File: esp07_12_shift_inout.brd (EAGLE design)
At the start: 100 x 45 mm, 47 parts, among them IC1 74HCT595D, IC2 74HCT595D, IC3 74HC165D, IC4 74HC165D

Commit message: First version vhich will go to production
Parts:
- moved JP11 10.2 mm to (3.17, 6.35)
- moved JP12 10.2 mm to (3.17, 8.89)
- moved JP7 10.2 mm to (3.17, 2.54)
- moved JP10 8.25 mm to (3.17, 12.7)
- moved JP8 8.25 mm to (3.17, 33.0)
- moved JP9 8.25 mm to (3.17, 43.2)
- moved R3 1.91 mm to (62.2, 42.5)
- moved C1 1.91 mm to (29.8, 7.62)
- moved C3 1.91 mm to (32.4, 7.62)
- moved C4 1.91 mm to (21.0, 5.08)
- moved C5 1.91 mm to (26.0, 5.08)
- moved D1 1.91 mm to (17.1, 5.08)
- moved IC1 1.91 mm to (58.4, 12.1)
- moved IC2 1.91 mm to (81.3, 12.1)
- moved IC3 1.91 mm to (58.4, 26.0)
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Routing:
- net VCC: track 318.1 -> 330.8 mm
- net GPIO16: track 31.6 -> 41.9 mm
- net VCC-5V: track 9.36 -> 18.5 mm
- net CH_PD: track 26.8 -> 34.6 mm
- net GPIO0: track 30.9 -> 38.6 mm
- net GPIO2: track 30.5 -> 37.5 mm
- net RXD: track 21.3 -> 27.6 mm
- net TXD: track 17.2 -> 23.1 mm
- net GPIO15: track 51.0 -> 55.9 mm
- net GND: track 328.2 -> 332.7 mm
- net SCK: track 122.5 -> 124.3 mm
- net IN_LATCH: track 91.6 -> 92.8 mm
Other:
- board size 100 x 45 mm -> 97 x 45 mm

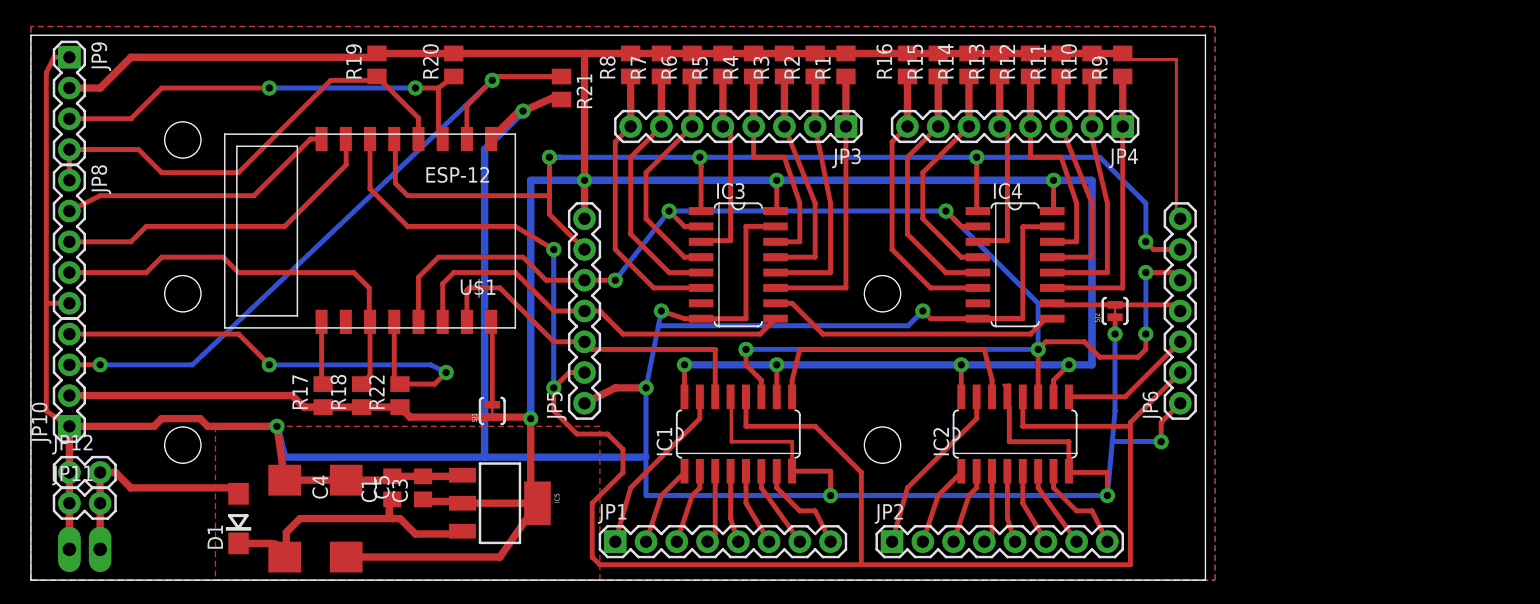
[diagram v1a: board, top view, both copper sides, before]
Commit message: * Change ESP module to ESP-12E footprint. Change ESP resistors to 0603. Change *_LATCH pins to 15,16
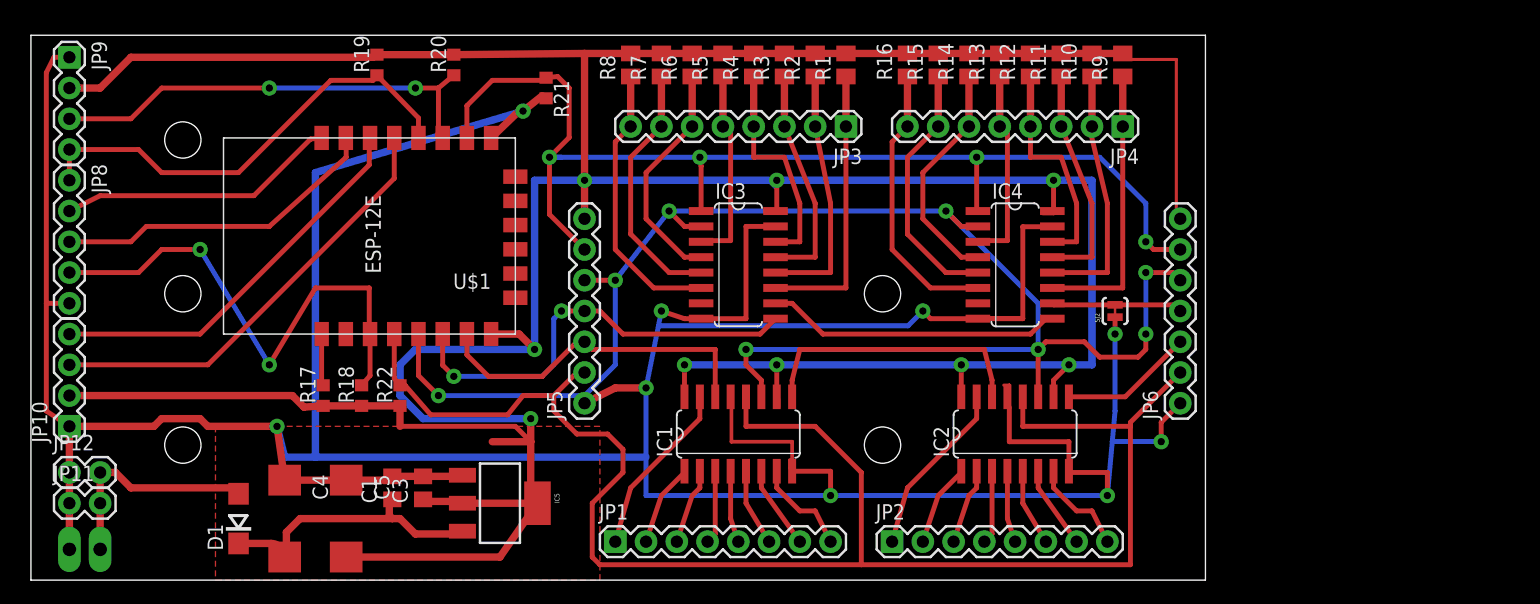
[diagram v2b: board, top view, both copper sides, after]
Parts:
- removed SJ1: SOLDERJUMPERTRACE, SparkFun-Retired:SJ_2S-TRACE
- R17, R18, R19, R20, R21, R22: device rcl:M0805 -> rcl:R0603
- U$1: value ESP8266_ESP-12 -> (none); device esp8266_esp12:EPS8266_ESP12 -> ESP8266-ESP12E:ESP8266-ESP12E
- moved U$1 16.5 mm to (40.0, 20.3)
- moved R21 1.27 mm to (42.5, 40.6)
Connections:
- removed net GPIO15: JP10.3, R21.1, U$1.2
- removed net GPIO16: JP10.4, R22.2, U$1.12
- removed net N$36: SJ1.2, U$1.16
- new net GPIO4: JP10.3, U$1.13
- new net GPIO5: JP10.4, U$1.14
- new net N$35: U$1.17
- new net N$37: U$1.18
- new net N$38: U$1.19
- new net N$39: U$1.20
- new net N$40: U$1.21
- new net N$41: U$1.22
- net ADC: now also U$1.2; no longer U$1.10
- net CH_PD: now also U$1.3; no longer U$1.11
- net GND: now also U$1.9; no longer U$1.1
- net GPIO0: now also U$1.12; no longer U$1.4
- net GPIO2: now also U$1.11; no longer U$1.3
- net IN_LATCH: now also R21.1, U$1.10; no longer U$1.5
- net MISO: now also U$1.6; no longer U$1.14
- net MOSI: now also U$1.7; no longer U$1.15
- net OUT_LATCH: now also R22.2, U$1.4; no longer U$1.6
- net REST: now also U$1.1; no longer U$1.9
- net RXD: now also U$1.15; no longer U$1.7
- net SCK: now also U$1.5; no longer U$1.13
- net TXD: now also U$1.16; no longer U$1.8
- net VCC: now also U$1.8; no longer SJ1.1
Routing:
- net GPIO15: track 55.9 -> 0.00 mm, vias 2 -> 0
- net GPIO16: track 41.9 -> 0.00 mm, vias 2 -> 0
- net GPIO4: track 0.00 -> 36.5 mm
- net GPIO5: track 0.00 -> 32.8 mm
- net VCC: track 330.8 -> 359.6 mm, vias 8 -> 9
- net OUT_LATCH: track 149.3 -> 135.3 mm, vias 2 -> 0
- net GND: track 332.7 -> 342.9 mm
- net SCK: track 124.3 -> 133.8 mm, vias 7 -> 8
- net CH_PD: track 34.6 -> 42.9 mm, vias 0 -> 2
- net N$36: track 6.89 -> 0.00 mm
- net MISO: track 33.6 -> 36.2 mm, vias 0 -> 2
- net IN_LATCH: track 92.8 -> 94.8 mm
- net REST: track 5.19 -> 4.26 mm
- net MOSI: track 29.2 -> 28.3 mm
- removed copper zone on layer 1, net GND
- removed copper zone on layer 16, net GND

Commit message: * Change OUT connectors to 2x10 and add GND / VCC pins to them
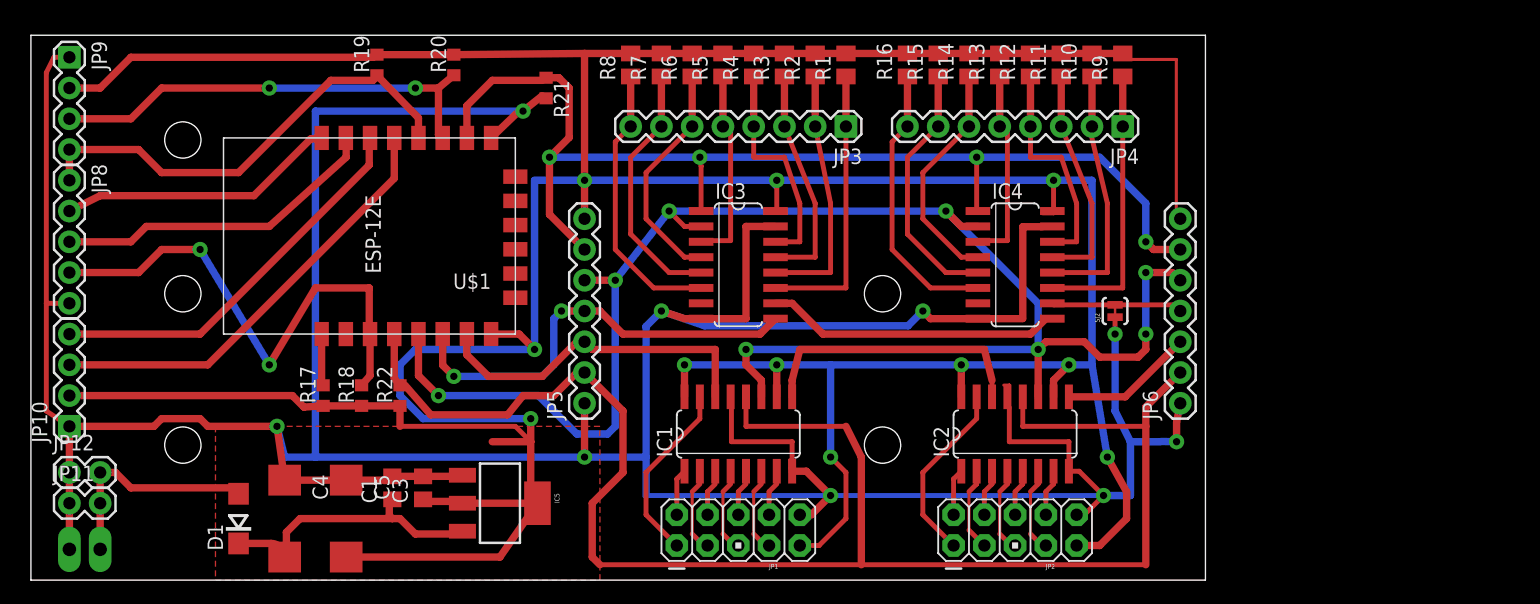
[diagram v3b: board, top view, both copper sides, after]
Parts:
- JP1, JP2: device SparkFun-Connectors:1X08 -> SparkFun-Connectors:AVR_ICSP
- moved JP1 10.2 mm to (58.4, 4.13), turned to 90 degrees
- moved JP2 10.2 mm to (81.3, 4.13), turned to 90 degrees
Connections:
- net N$10 renamed OUT8
- net N$11 renamed OUT9
- net N$12 renamed OUT10
- net N$13 renamed OUT11
- net N$14 renamed OUT12
- net N$15 renamed OUT13
- net N$16 renamed OUT14
- net N$17 renamed OUT15
- net N$18 renamed OUT16
- net N$3 renamed OUT1
- net N$4 renamed OUT2
- net N$5 renamed OUT3
- net N$6 renamed OUT4
- net N$7 renamed OUT5
- net N$8 renamed OUT6
- net N$9 renamed OUT7
- net GND: now also JP1.10, JP2.10
- net VCC: now also JP1.9, JP2.9
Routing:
- net VCC: track 359.6 -> 395.8 mm, vias 9 -> 11
- net GND: track 342.9 -> 351.4 mm
- net SCK: track 133.8 -> 139.5 mm
- net OUT8: track 8.18 -> 3.86 mm
- net OUT16: track 8.18 -> 3.86 mm
- net OUT2: track 6.81 -> 3.86 mm
- net OUT10: track 6.81 -> 3.86 mm
- net OUT_LATCH: track 135.3 -> 138.0 mm
- net OUT6: track 6.34 -> 3.86 mm
- net OUT14: track 6.34 -> 3.86 mm
- net OUT12: track 6.08 -> 3.86 mm
- net OUT4: track 6.08 -> 3.86 mm
- net OUT5: track 5.92 -> 7.11 mm
- net OUT13: track 5.92 -> 7.11 mm
- net OUT3: track 6.29 -> 7.11 mm
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
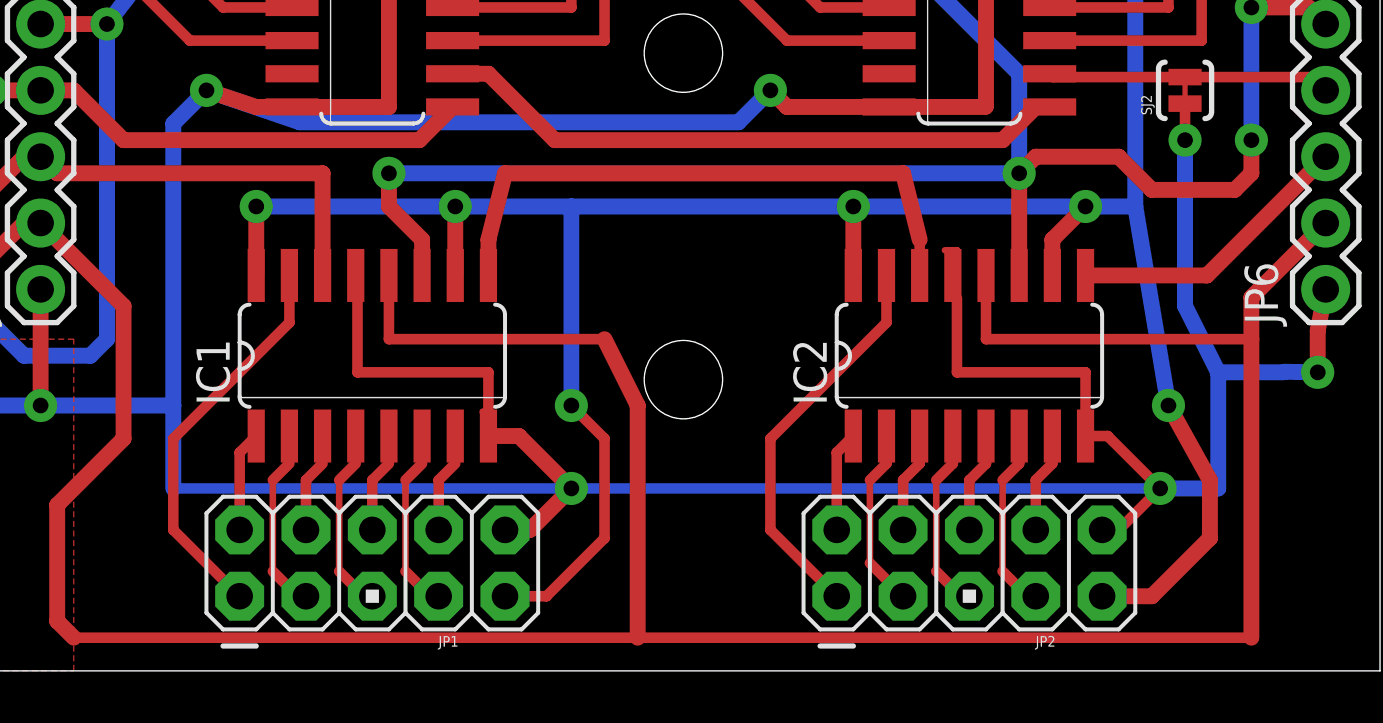
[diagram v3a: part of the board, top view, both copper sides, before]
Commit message: * Change OUT pins configuration to pin 1 - GND, pin 10 - VCC
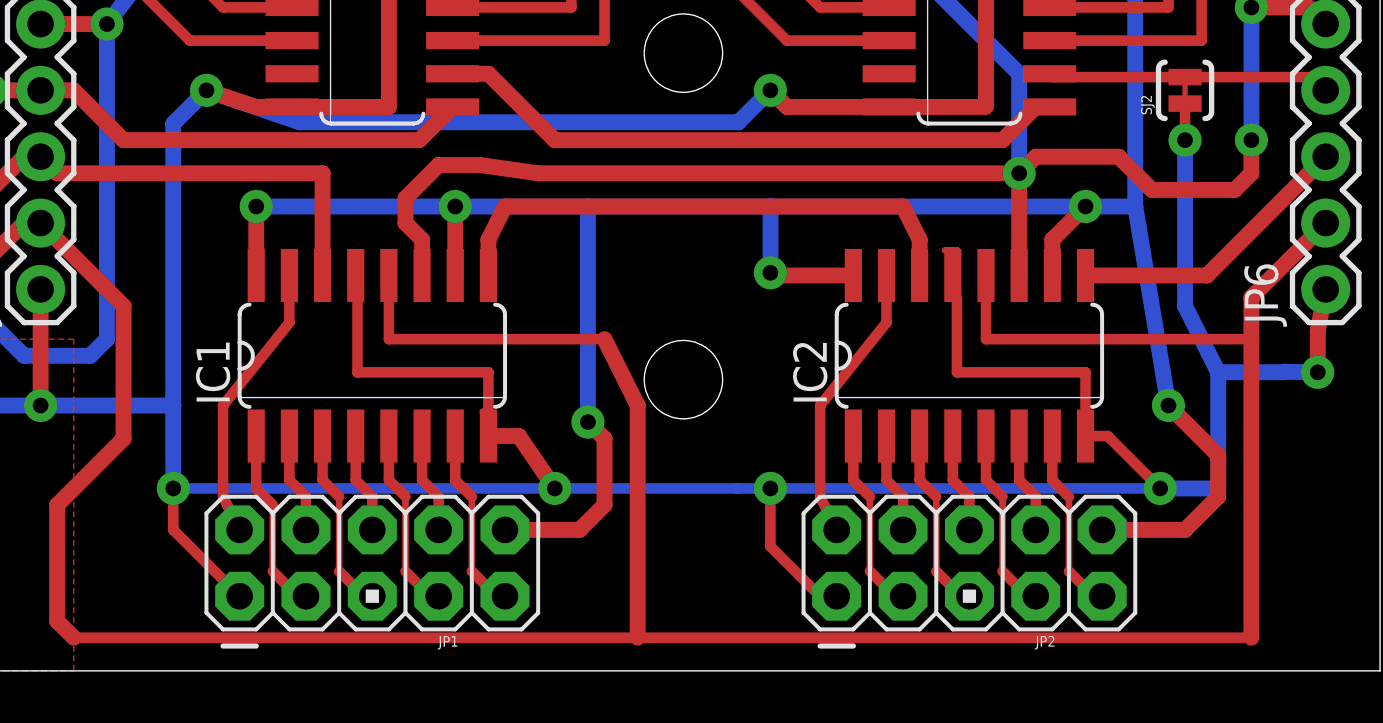
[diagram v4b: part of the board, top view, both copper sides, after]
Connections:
- net GND: now also JP1.1, JP2.1; no longer JP1.10, JP2.10
- net OUT1: now also JP1.2; no longer JP1.1
- net OUT10: now also JP2.3; no longer JP2.2
- net OUT11: now also JP2.4; no longer JP2.3
- net OUT12: now also JP2.5; no longer JP2.4
- net OUT13: now also JP2.6; no longer JP2.5
- net OUT14: now also JP2.7; no longer JP2.6
- net OUT15: now also JP2.8; no longer JP2.7
- net OUT16: now also JP2.9; no longer JP2.8
- net OUT2: now also JP1.3; no longer JP1.2
- net OUT3: now also JP1.4; no longer JP1.3
- net OUT4: now also JP1.5; no longer JP1.4
- net OUT5: now also JP1.6; no longer JP1.5
- net OUT6: now also JP1.7; no longer JP1.6
- net OUT7: now also JP1.8; no longer JP1.7
- net OUT8: now also JP1.9; no longer JP1.8
- net OUT9: now also JP2.2; no longer JP2.1
- net VCC: now also JP1.10, JP2.10; no longer JP1.9, JP2.9
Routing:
- net OUT9: track 15.2 -> 10.8 mm
- net OUT1: track 15.2 -> 10.8 mm
- net GND: track 351.4 -> 355.6 mm, vias 9 -> 11
- net OUT7: track 7.11 -> 3.86 mm
- net OUT15: track 7.11 -> 3.86 mm
- net OUT10: track 3.86 -> 7.11 mm
- net OUT8: track 3.86 -> 7.11 mm
- net OUT6: track 3.86 -> 7.11 mm
- net OUT4: track 3.86 -> 7.11 mm
- net OUT2: track 3.86 -> 7.11 mm
- net OUT5: track 7.11 -> 3.86 mm
- net OUT3: track 7.11 -> 3.86 mm
- net OUT16: track 3.86 -> 7.11 mm
- net OUT12: track 3.86 -> 7.11 mm
- net OUT14: track 3.86 -> 7.11 mm
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
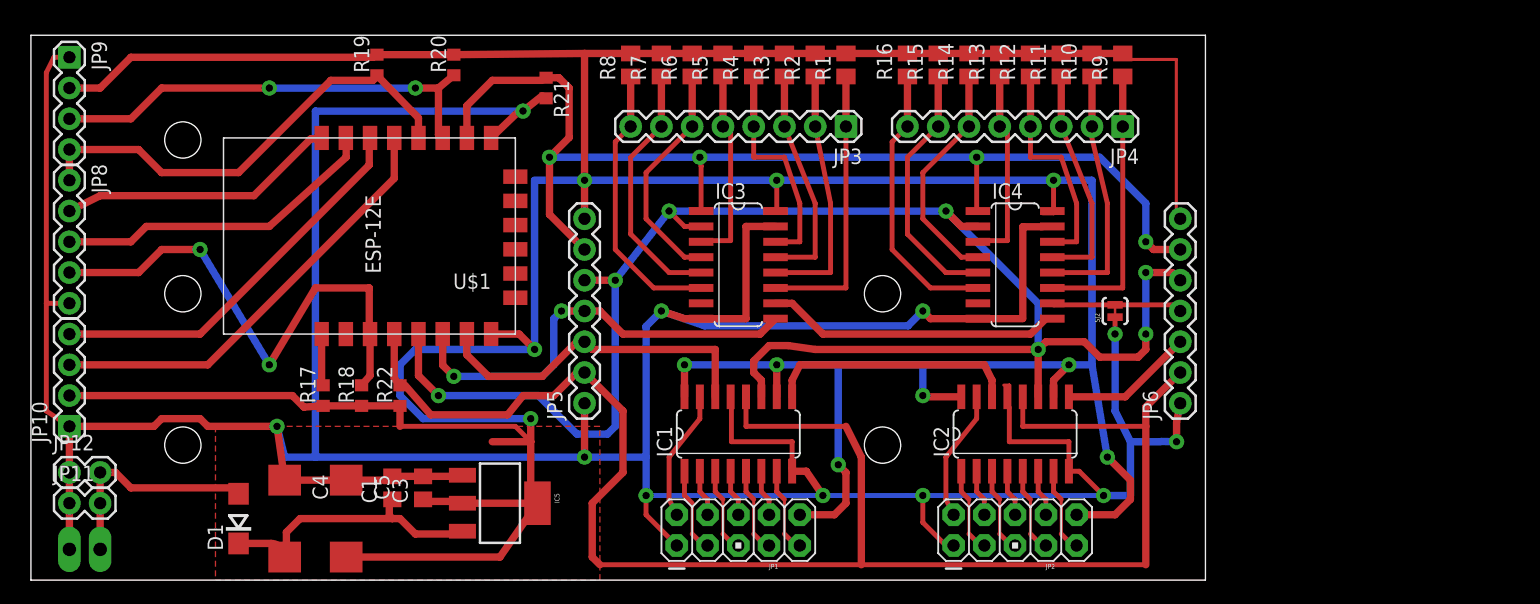
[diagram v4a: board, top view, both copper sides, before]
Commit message: * Finish new version of PCB.
* Change ESP module to ESP-12E with additional (but useless) pins
* Change OUT_ IN_ latch to 15,16
* Change OUT_ IN_ connection to 2x5 header
* Remove pull-up resistors on IN_ part in favour to implement them in add-on opto-isolated IN PCB
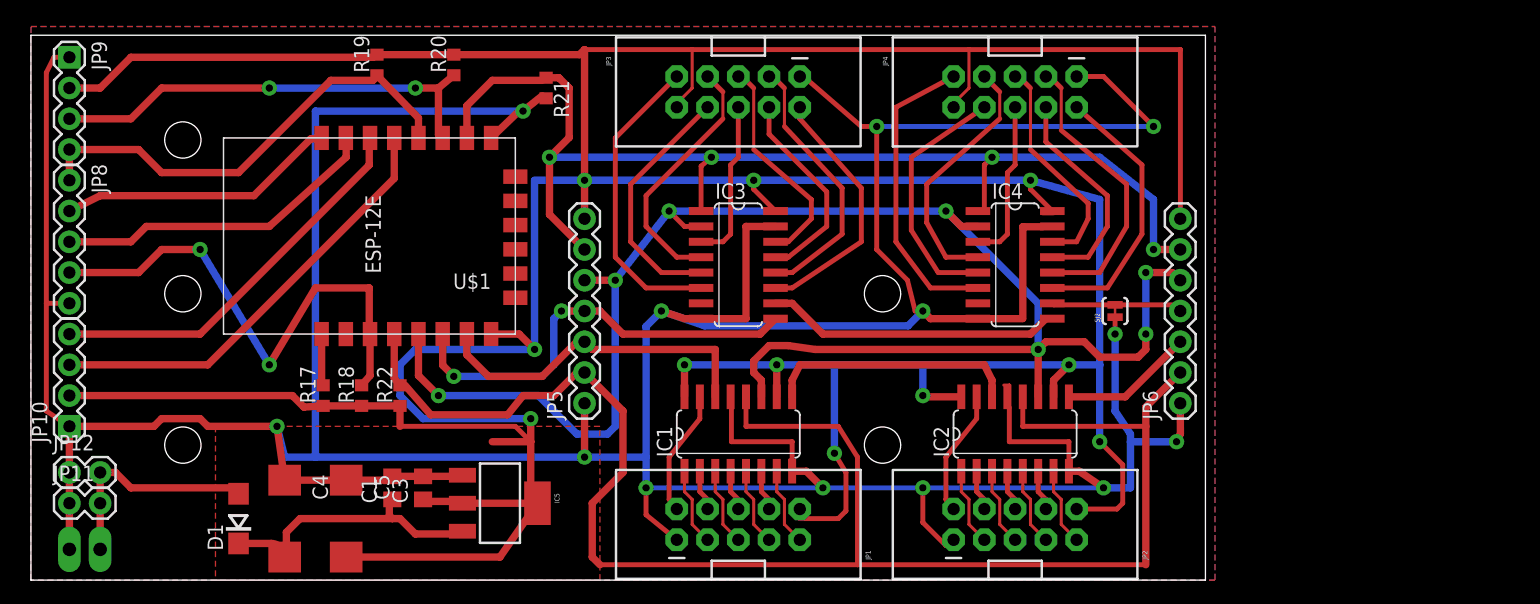
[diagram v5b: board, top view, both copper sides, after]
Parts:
- removed R1, R10, R11, R12, R13, R14, R15, R16, R2, R3, R4, R5, R6, R7, R8, R9: (no value), rcl:M0805
- JP1, JP2: device SparkFun-Connectors:AVR_ICSP -> SparkFun-Connectors:2X5-SHROUDED
- JP3, JP4: device SparkFun-Connectors:1X08 -> SparkFun-Connectors:2X5-SHROUDED
- moved JP3 9.34 mm to (58.4, 40.3), turned to 270 degrees
- moved JP4 9.34 mm to (81.3, 40.3), turned to 270 degrees
- moved JP1 0.47 mm to (58.4, 4.60)
- moved JP2 0.47 mm to (81.3, 4.60)
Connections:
- removed net N$19: IC3.11, JP3.1, R1.1
- removed net N$20: IC3.12, JP3.2, R2.1
- removed net N$21: IC3.13, JP3.3, R3.1
- removed net N$22: IC3.14, JP3.4, R4.1
- removed net N$23: IC3.3, JP3.5, R5.1
- removed net N$24: IC3.4, JP3.6, R6.1
- removed net N$25: IC3.5, JP3.7, R7.1
- removed net N$26: IC3.6, JP3.8, R8.1
- removed net N$27: IC4.11, JP4.1, R9.1
- removed net N$28: IC4.12, JP4.2, R10.1
- removed net N$29: IC4.13, JP4.3, R11.1
- removed net N$30: IC4.14, JP4.4, R12.1
- removed net N$31: IC4.3, JP4.5, R13.1
- removed net N$32: IC4.4, JP4.6, R14.1
- removed net N$33: IC4.5, JP4.7, R15.1
- removed net N$34: IC4.6, JP4.8, R16.1
- new net IN1: IC3.11, JP3.2
- new net IN10: IC4.12, JP4.3
- new net IN11: IC4.13, JP4.4
- new net IN12: IC4.14, JP4.5
- new net IN13: IC4.3, JP4.6
- new net IN14: IC4.4, JP4.7
- new net IN15: IC4.5, JP4.8
- new net IN16: IC4.6, JP4.9
- new net IN2: IC3.12, JP3.3
- new net IN3: IC3.13, JP3.4
- new net IN4: IC3.14, JP3.5
- new net IN5: IC3.3, JP3.6
- new net IN6: IC3.4, JP3.7
- new net IN7: IC3.5, JP3.8
- new net IN8: IC3.6, JP3.9
- new net IN9: IC4.11, JP4.2
- net GND: now also JP3.1, JP4.1
- net VCC: now also JP3.10, JP4.10; no longer R1.2, R10.2, R11.2, R12.2, R13.2, R14.2, R15.2, R16.2, R2.2, R3.2, R4.2, R5.2, R6.2, R7.2, R8.2, R9.2
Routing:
- net GND: track 355.6 -> 411.1 mm, vias 11 -> 13
- net IN16: track 0.00 -> 25.2 mm
- net IN8: track 0.00 -> 25.2 mm
- net IN10: track 0.00 -> 24.0 mm
- net N$27: track 23.3 -> 0.00 mm
- net N$19: track 23.3 -> 0.00 mm
- net N$26: track 23.2 -> 0.00 mm
- net N$34: track 23.2 -> 0.00 mm
- net IN9: track 0.00 -> 22.7 mm
- net IN2: track 0.00 -> 22.2 mm
- net N$28: track 21.8 -> 0.00 mm
- net IN1: track 0.00 -> 21.3 mm
- net N$25: track 21.2 -> 0.00 mm
- net N$33: track 21.2 -> 0.00 mm
- net IN14: track 0.00 -> 21.2 mm
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- added copper zone on layer 1, net GND
- added copper zone on layer 16, net GND
